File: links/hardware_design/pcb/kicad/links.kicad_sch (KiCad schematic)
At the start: 54 parts

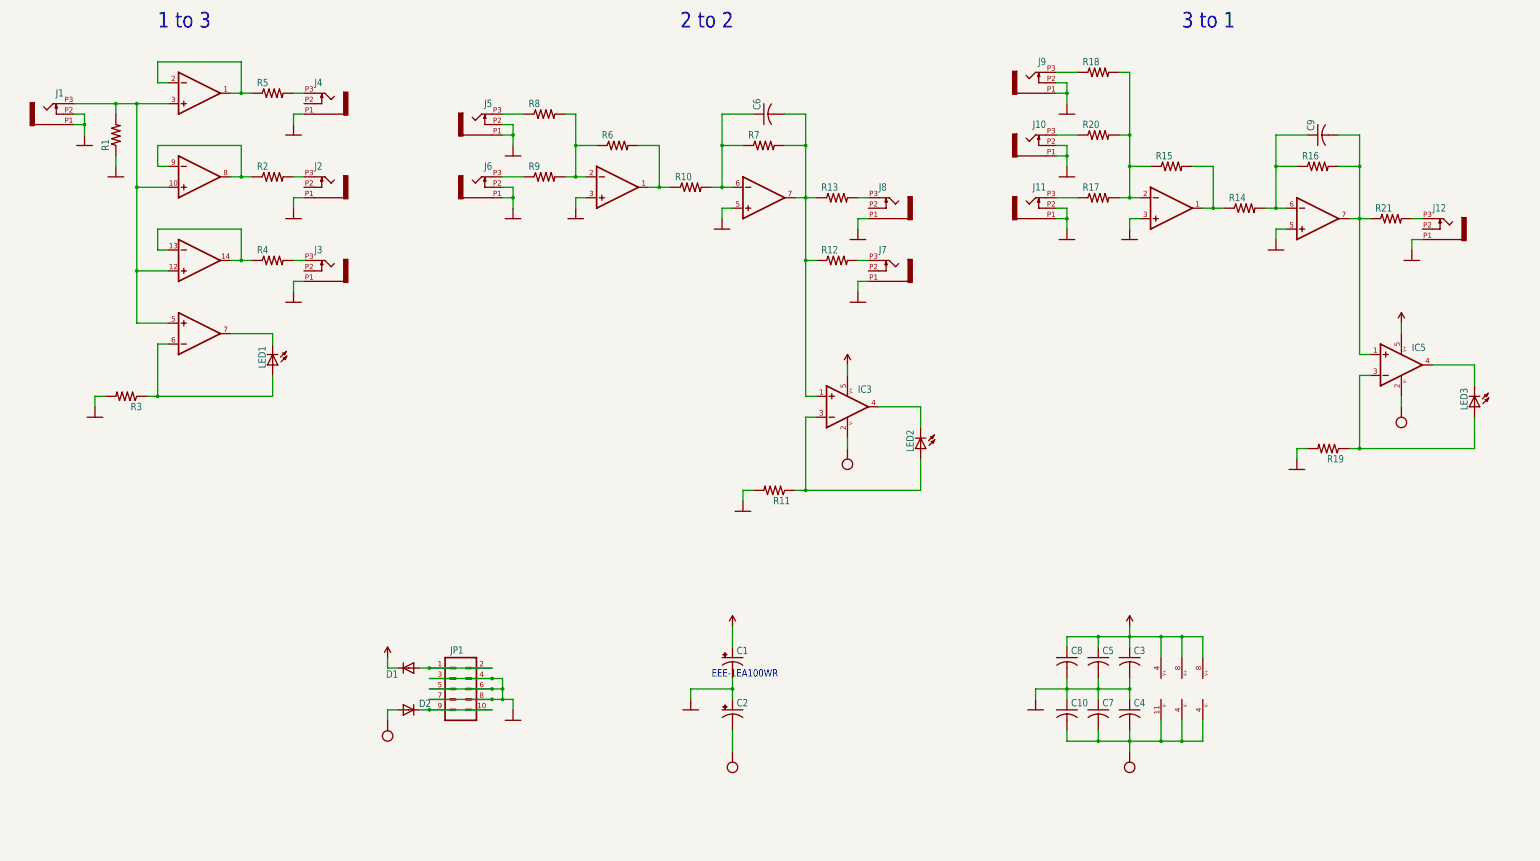
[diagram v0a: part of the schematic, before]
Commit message: links: move LEDs to left side
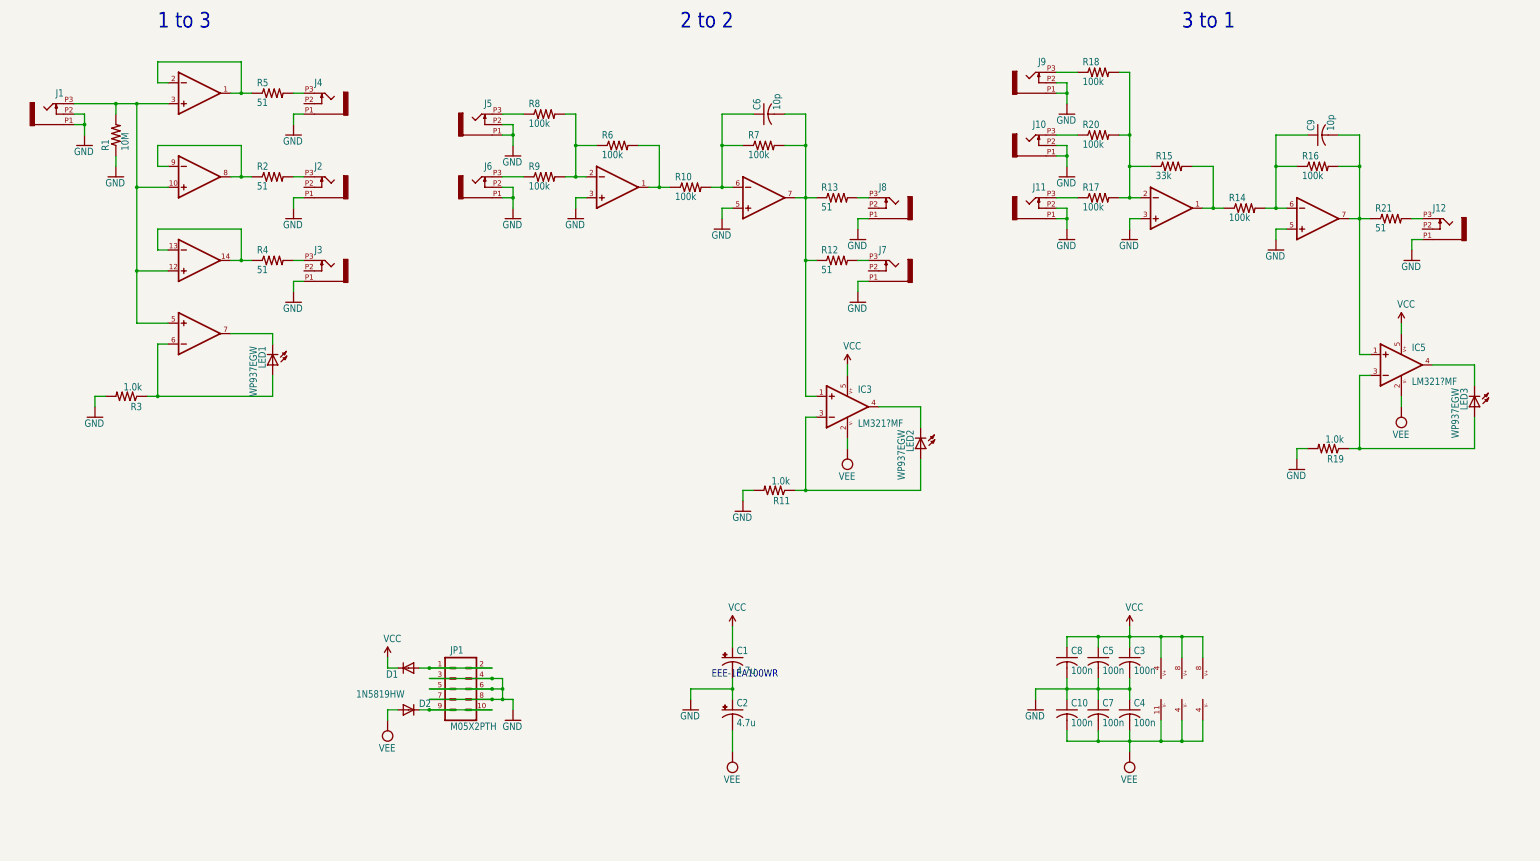
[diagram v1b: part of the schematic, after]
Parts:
- C1, C2: value (none) -> 4.7u; footprint (none) -> links:PANASONIC_A
- C10, C3, C4, C5, C7, C8: value (none) -> 100n; footprint (none) -> links:C0603
- C6, C9: value (none) -> 10p; footprint (none) -> links:C0603
- D1, D2: value (none) -> 1N5819HW; footprint (none) -> links:SOD123
- IC1: value (none) -> OPA4171; footprint (none) -> links:TSSOP14
- IC2, IC4: value (none) -> TL072PW; footprint (none) -> links:TSSOP8
- IC3, IC5: value (none) -> LM321?MF; footprint (none) -> links:SOT23-5
- J1, J10, J11, J12, J2, J3, J4, J5, J6, J7, J8, J9: value (none) -> PJ301_THONKICONN6; footprint (none) -> links:WQP_PJ_301M6
- JP1: value (none) -> M05X2PTH; footprint (none) -> links:AVR_ICSP
- LED1, LED2, LED3: value (none) -> WP937EGW; footprint (none) -> links:LED3MM
- R1: value (none) -> 10M; footprint (none) -> links:R0603
- R10, R14, R16, R17, R18, R20, R6, R7, R8, R9: value (none) -> 100k; footprint (none) -> links:R0603
- R11, R19, R3: value (none) -> 1.0k; footprint (none) -> links:R0603
- R12, R13, R2, R21, R4, R5: value (none) -> 51; footprint (none) -> links:R0603
- R15: value (none) -> 33k; footprint (none) -> links:R0603

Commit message: links: change panasonic A to 3x5.3mm footprint
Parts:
- C1, C2: footprint links:PANASONIC_A -> Capacitor_SMD:CP_Elec_3x5.3
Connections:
- net GND: now also C1.2, C2.1; no longer C1.-, C2.+
- net VCC: now also C1.1; no longer C1.+
- net VEE: now also C2.2; no longer C2.-
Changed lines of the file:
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@@
       (effects (font (size 1.778 1.5113)) (justify left bottom))
     )
-    (property "Footprint" "links:PANASONIC_A" (at 200.66 198.12 0)
+    (property "Footprint" "Capacitor_SMD:CP_Elec_3x5.3" (at 200.66 198.12 0)
       (effects (font (size 1.27 1.27)) hide)
     )
@@
       (effects (font (size 1.27 1.27)) hide)
     )
-    (pin "+")
-    (pin "-")
+    (pin "1")
+    (pin "2")
     (instances
       (project "links"
@@
       (effects (font (size 1.778 1.5113)) (justify left bottom))
     )
-    (property "Footprint" "links:PANASONIC_A" (at 200.66 185.42 0)
+    (property "Footprint" "Capacitor_SMD:CP_Elec_3x5.3" (at 200.66 185.42 0)
       (effects (font (size 1.27 1.27)) hide)
     )
@@
       (effects (font (size 1.27 1.27)) hide)
     )
-    (pin "+")
-    (pin "-")
-    (instances
-      (project "links"
+    (pin "1")
+    (pin "2")
+    (instances
+      (project "links"
